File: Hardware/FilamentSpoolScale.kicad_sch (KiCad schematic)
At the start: 14 parts, among them J1 0.91 inch OLED, J2 Load Cell, J3 Screw_Terminal_01x02, J4 Conn_01x03, SW1 SW_Push

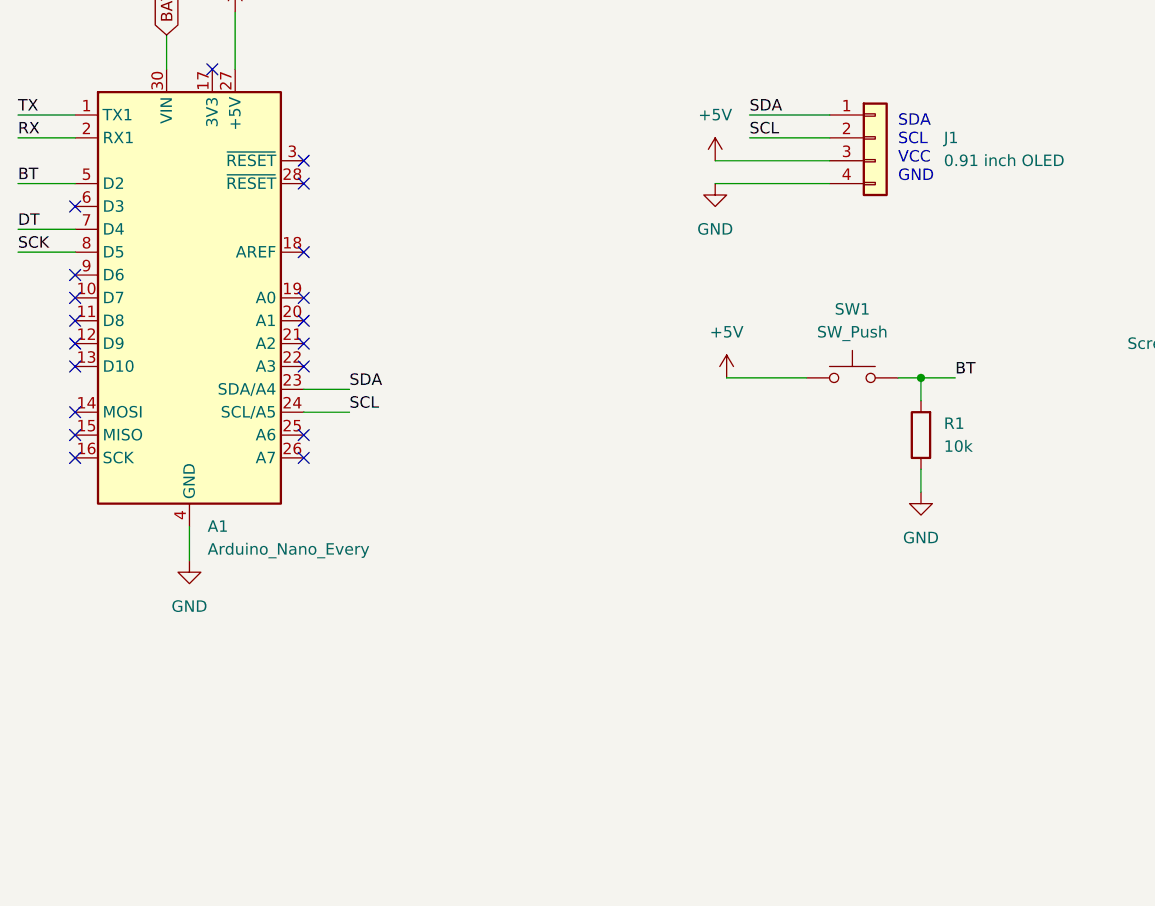
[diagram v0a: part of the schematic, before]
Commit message: Addition of 2nd button (backup button)
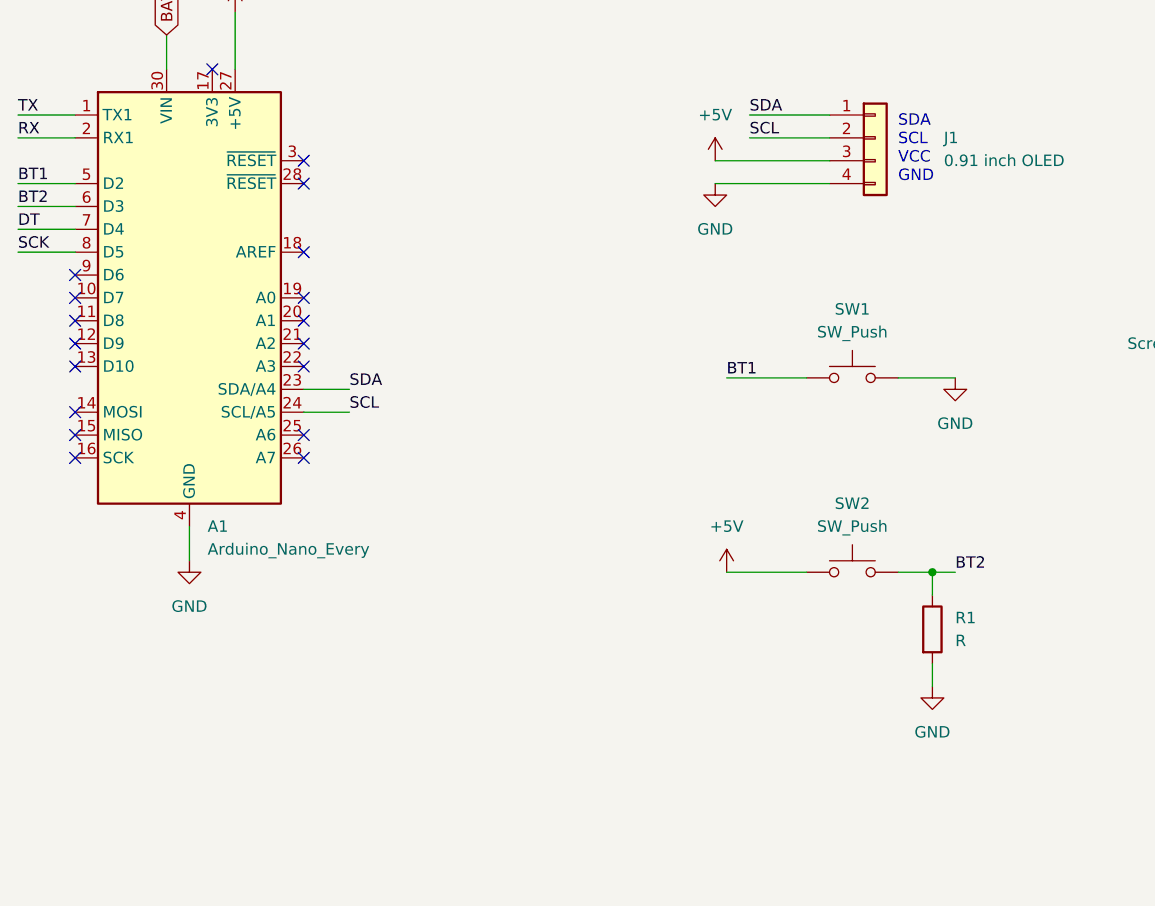
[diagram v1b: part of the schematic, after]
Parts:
- added SW2: SW_Push, Button_Switch_THT:SW_PUSH_6mm_H4.3mm, symbol Switch:SW_Push
- R1: value 10k -> R; footprint Resistor_THT:R_Axial_DIN0207_L6.3mm_D2.5mm_P7.62mm_Horizontal -> Resistor_THT:R_Axial_DIN0207_L6.3mm_D2.5mm_P10.16mm_Horizontal
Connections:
- net +5V: now also SW2.1; no longer SW1.1
- net GND: now also R1.2, SW1.2; no longer R1.1
- net BT2: now reaches A1.6 (D3)
- net BT2: now also R1.1, SW2.2
- removed net BT: A1.5 (D2), R1.2, SW1.2
- new net BT1: A1.5 (D2), SW1.1
- no-connect marks 19 -> 18

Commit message: Board design
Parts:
- added J5: Conn_01x06, Connector_PinHeader_2.54mm:PinHeader_1x06_P2.54mm_Vertical, symbol Connector_Generic:Conn_01x06
- added J6: Conn_01x06, Connector_PinHeader_2.54mm:PinHeader_1x06_P2.54mm_Horizontal, symbol Connector_Generic:Conn_01x06
- H1, H2, H3, H4, H5, H6: footprint (none) -> MountingHole:MountingHole_3.2mm_M3_DIN965_Pad_TopBottom
- J4: footprint (none) -> Connector_PinHeader_2.54mm:PinHeader_1x03_P2.54mm_Vertical
- R1: value R -> 10k
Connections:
- net +5V: now also J5.3 (Pin_3), J6.3 (Pin_3)
- net BT1: now also J5.5 (Pin_5), J6.5 (Pin_5)
- net BT2: now also J5.6 (Pin_6), J6.6 (Pin_6)
- net GND: now also J5.4 (Pin_4), J6.4 (Pin_4)
- net SCL: now also J5.2 (Pin_2), J6.2 (Pin_2)
- net SDA: now also J5.1 (Pin_1), J6.1 (Pin_1)
